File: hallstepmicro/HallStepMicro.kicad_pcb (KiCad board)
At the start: 2 copper layers, 25.4 x 55.9 mm, 30 parts, among them IC1 ATTINY84A-SS

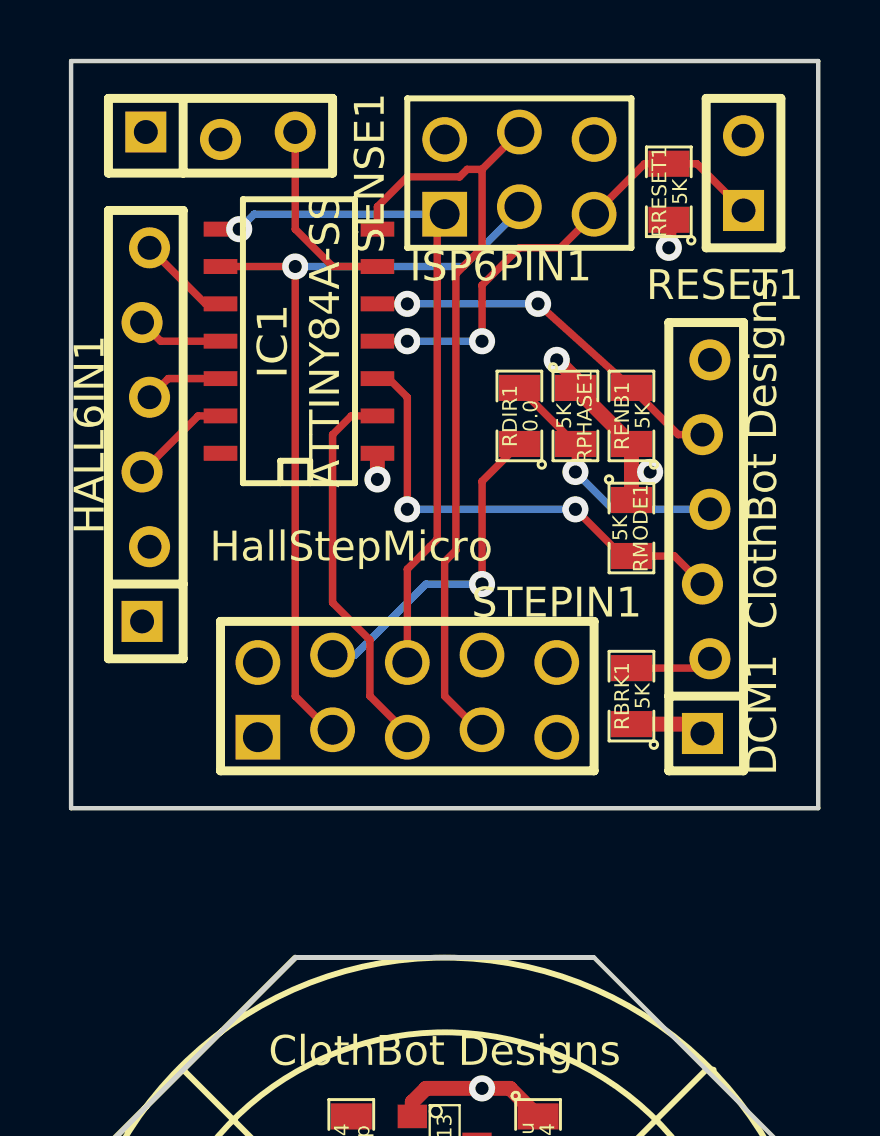
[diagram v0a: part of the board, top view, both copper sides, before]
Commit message: Moving two boards against each other.
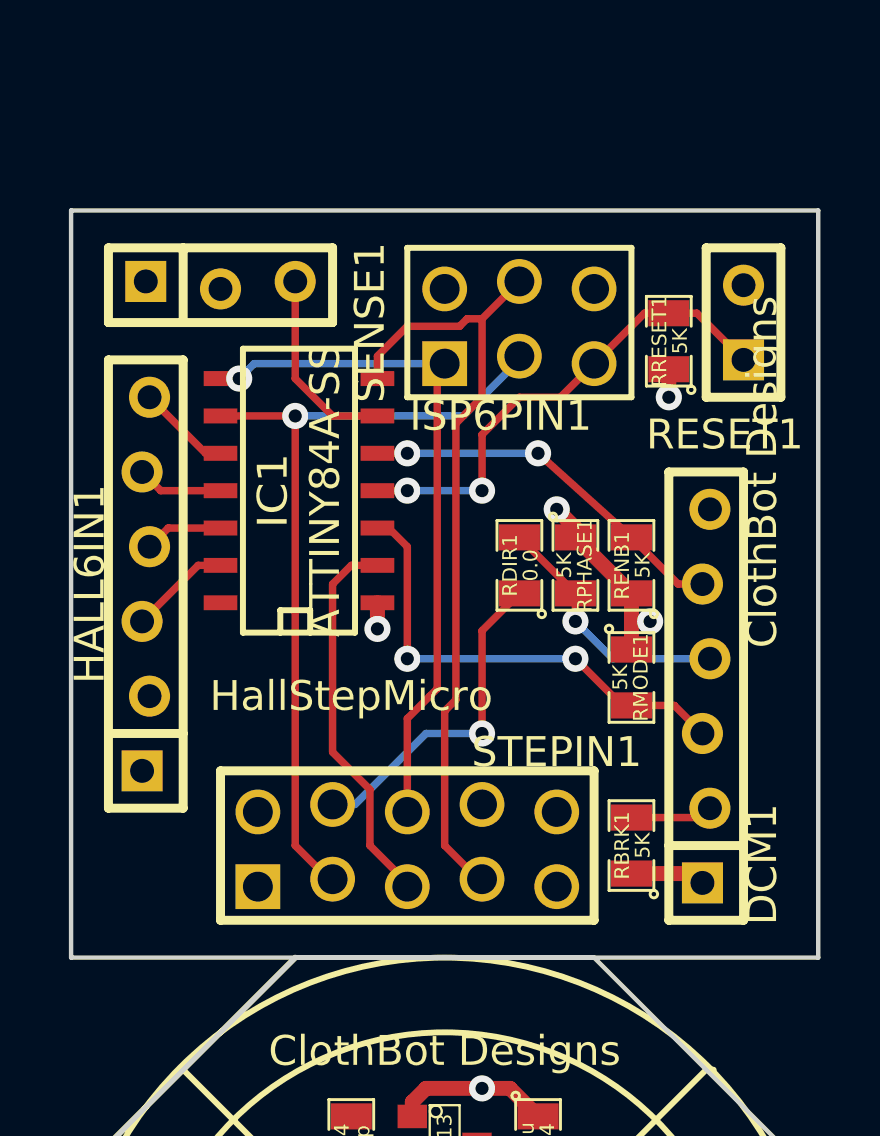
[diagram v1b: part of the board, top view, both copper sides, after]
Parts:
- moved DCM1 5.08 mm to (135.9, 54.6)
- moved HALL6IN1 5.08 mm to (116.8, 50.8)
- moved IC1 5.08 mm to (121.9, 47.6)
- moved ISP6PIN1 5.08 mm to (129.5, 41.9)
- moved RBRK1 5.08 mm to (133.3, 59.7)
- moved RDIR1 5.08 mm to (129.5, 50.2)
- moved RENB1 5.08 mm to (133.3, 50.2)
- moved RESET1 5.08 mm to (137.2, 41.9)
- moved RMODE1 5.08 mm to (133.3, 54.0)
- moved RPHASE1 5.08 mm to (131.4, 50.2)
- moved RRESET1 5.08 mm to (134.6, 42.5)
- moved SENSE1 5.08 mm to (119.4, 40.6)
- moved STEPIN1 5.08 mm to (125.7, 59.7)
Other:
- board size 25.4 x 55.9 mm -> 25.4 x 50.8 mm

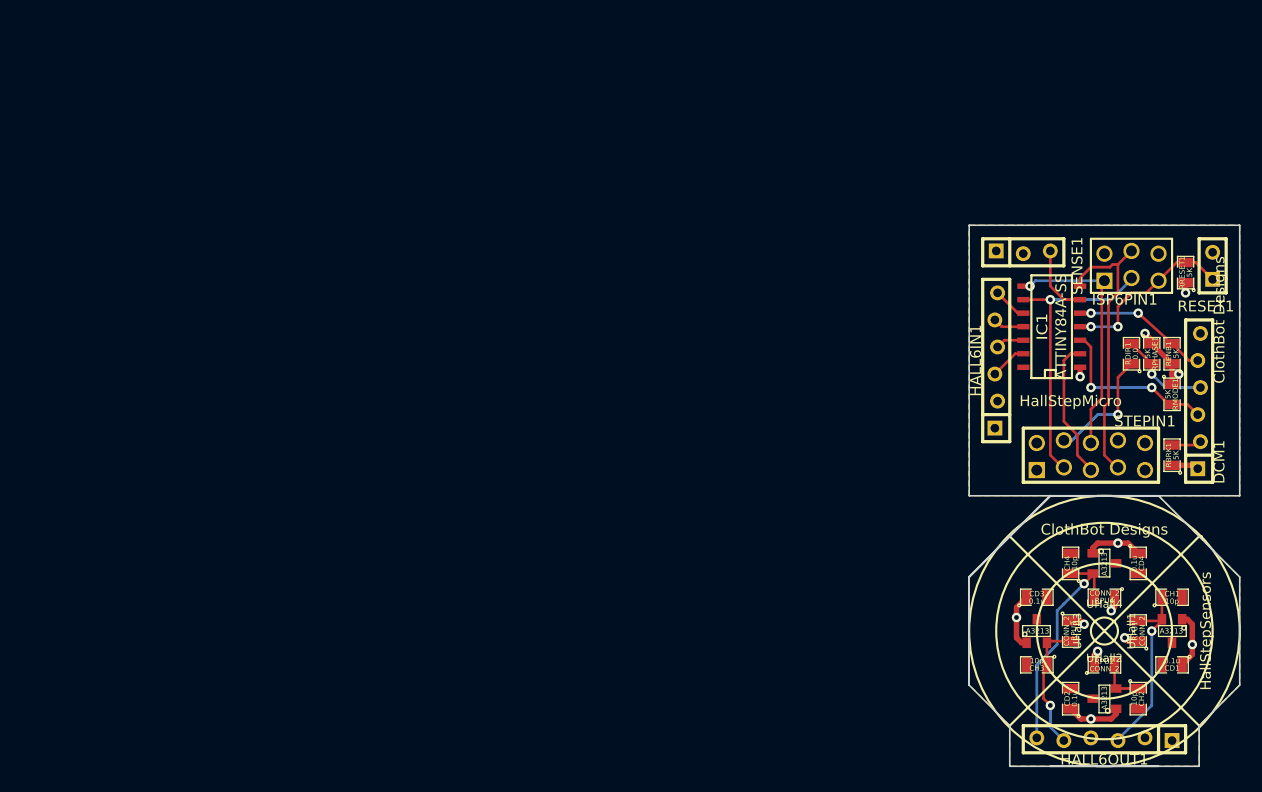
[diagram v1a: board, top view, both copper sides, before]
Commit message: Repositioned boards for right-angle cuts and cleaned up silkscreen layers.
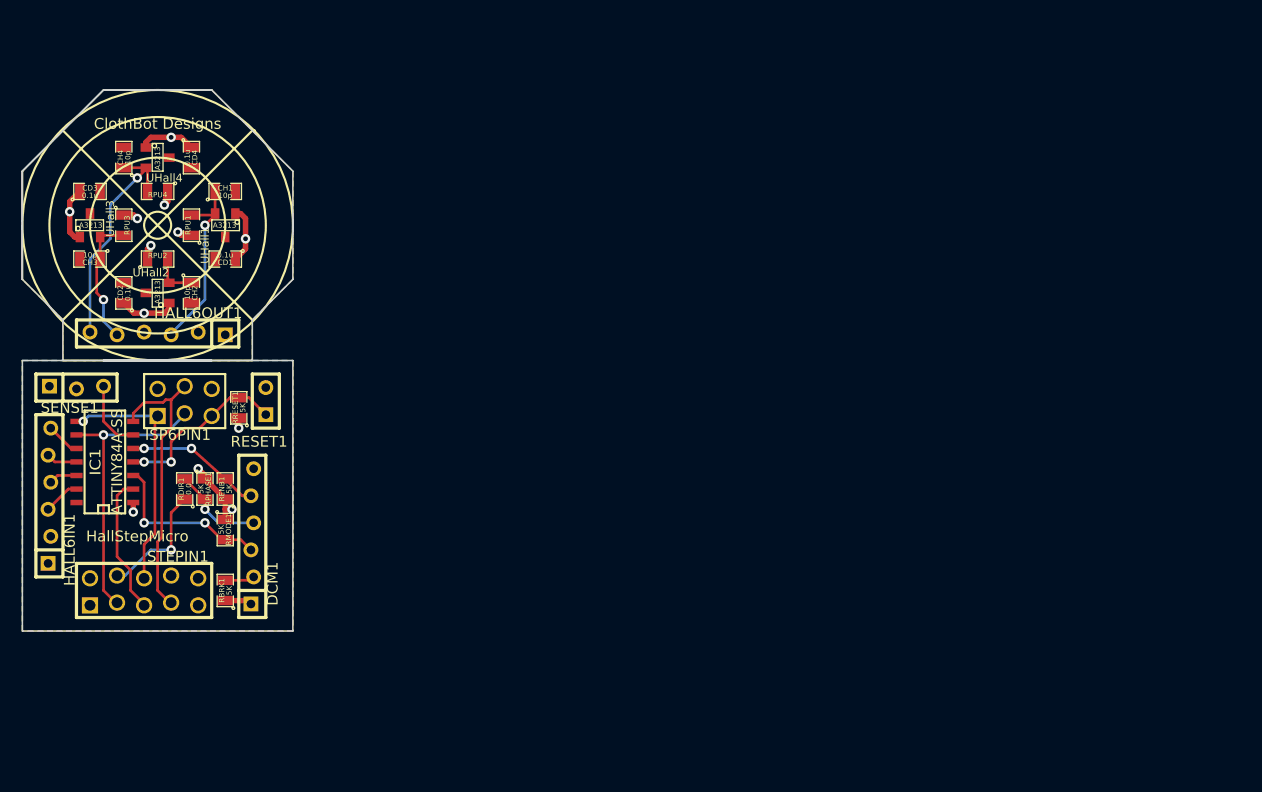
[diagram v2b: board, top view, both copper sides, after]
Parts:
- moved CD2 96.7 mm to (34.9, 44.5)
- moved CD3 96.7 mm to (31.8, 34.9)
- moved CD4 96.7 mm to (41.3, 31.8)
- moved CH2 96.7 mm to (41.3, 44.5)
- moved CH3 96.7 mm to (31.8, 41.3)
- moved CH4 96.7 mm to (34.9, 31.8)
- moved HALL6OUT1 96.7 mm to (38.1, 48.3)
- moved RPU1 96.7 mm to (41.3, 38.1)
- moved RPU2 96.7 mm to (38.1, 41.3)
- moved RPU3 96.7 mm to (34.9, 38.1)
- moved RPU4 96.7 mm to (38.1, 34.9)
- moved UHall2 96.7 mm to (38.1, 44.5)
- moved UHall3 96.7 mm to (31.8, 38.1)
- moved UHall4 96.7 mm to (38.1, 31.8)
- moved CD1 96.7 mm to (44.5, 41.3)
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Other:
- outline, holes or cut-outs redrawn

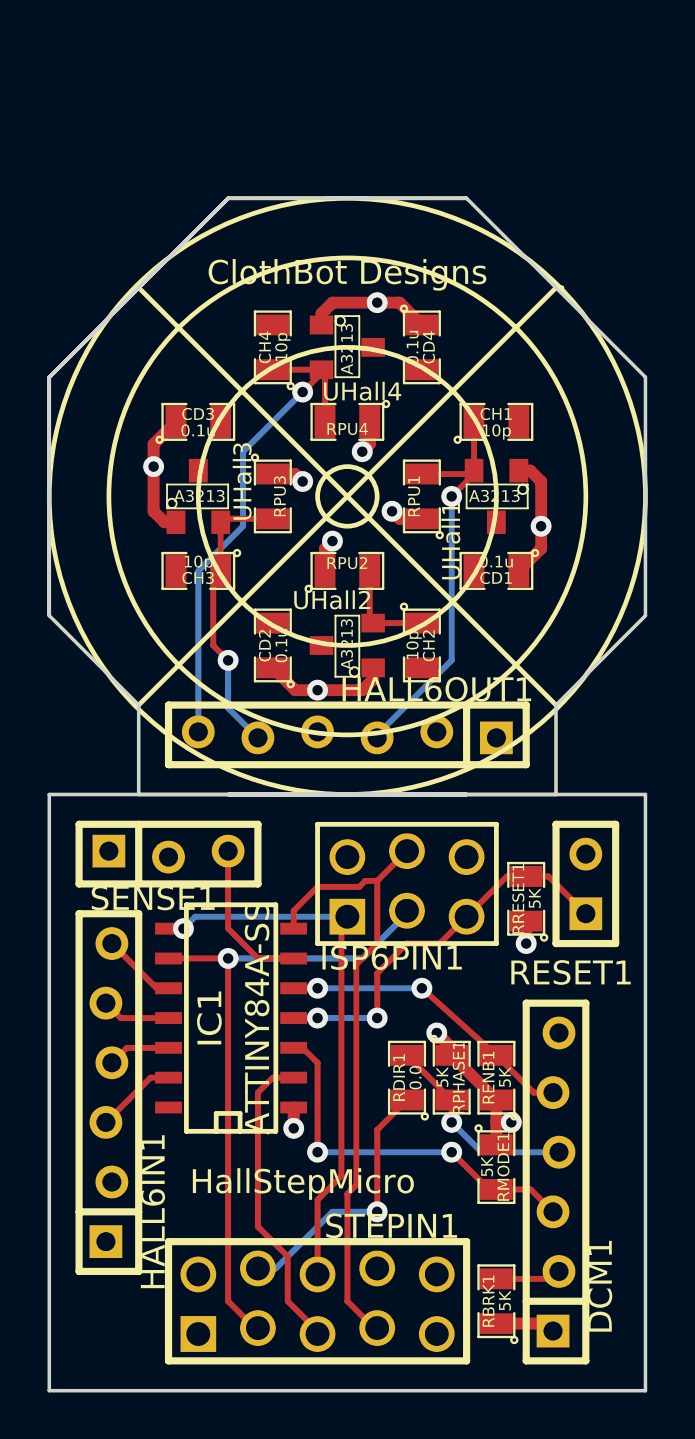
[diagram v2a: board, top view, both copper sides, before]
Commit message: Resizing edges to come under 2"x1"
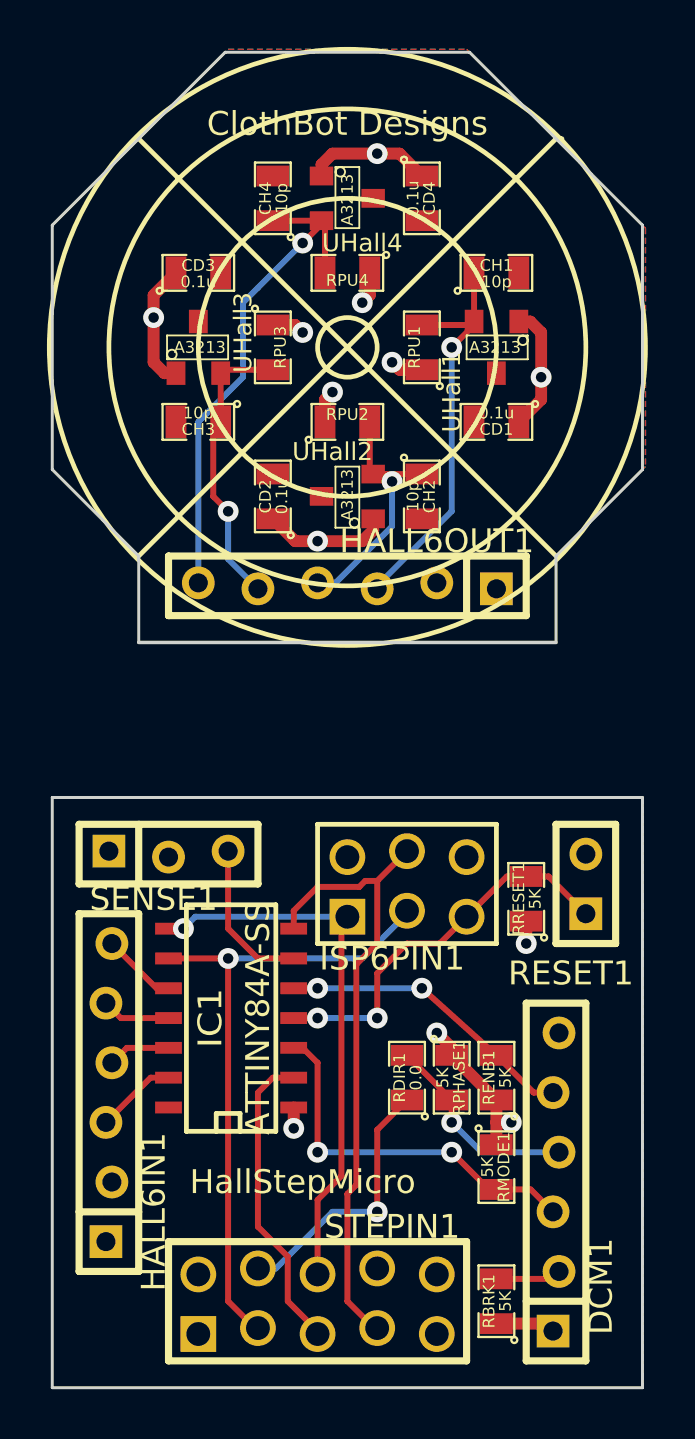
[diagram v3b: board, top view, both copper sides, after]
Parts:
- moved CD1 6.35 mm to (44.5, 34.9)
- moved CD2 6.35 mm to (34.9, 38.1)
- moved CD4 6.35 mm to (41.3, 25.4)
- moved CH2 6.35 mm to (41.3, 38.1)
- moved CH3 6.35 mm to (31.8, 34.9)
- moved CH4 6.35 mm to (34.9, 25.4)
- moved HALL6OUT1 6.35 mm to (38.1, 41.9)
- moved RPU1 6.35 mm to (41.3, 31.8)
- moved RPU2 6.35 mm to (38.1, 34.9)
- moved RPU3 6.35 mm to (34.9, 31.8)
- moved UHall1 6.35 mm to (44.5, 31.8)
- moved UHall2 6.35 mm to (38.1, 38.1)
- moved UHall3 6.35 mm to (31.8, 31.8)
- moved UHall4 6.35 mm to (38.1, 25.4)
- moved CD3 6.35 mm to (31.8, 28.6)
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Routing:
- net /HallSensors1/hall2: track 4.36 -> 11.4 mm, vias 0 -> 1
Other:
- board size 25.4 x 50.8 mm -> 25.1 x 56.9 mm

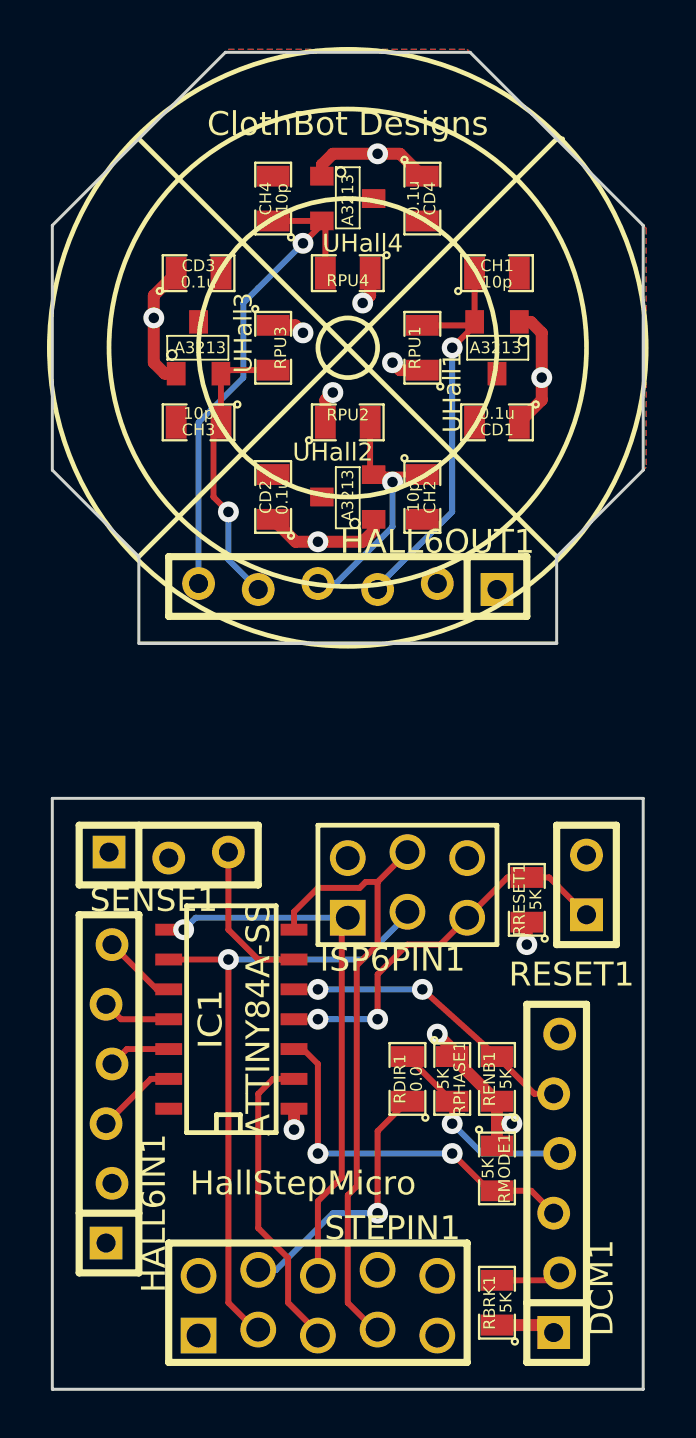
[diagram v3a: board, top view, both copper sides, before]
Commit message: Added extra clearance to copper pour
Dimension problem was probably too-large silk screen, but explicitly
satisfying DRC is a good thing anyway.
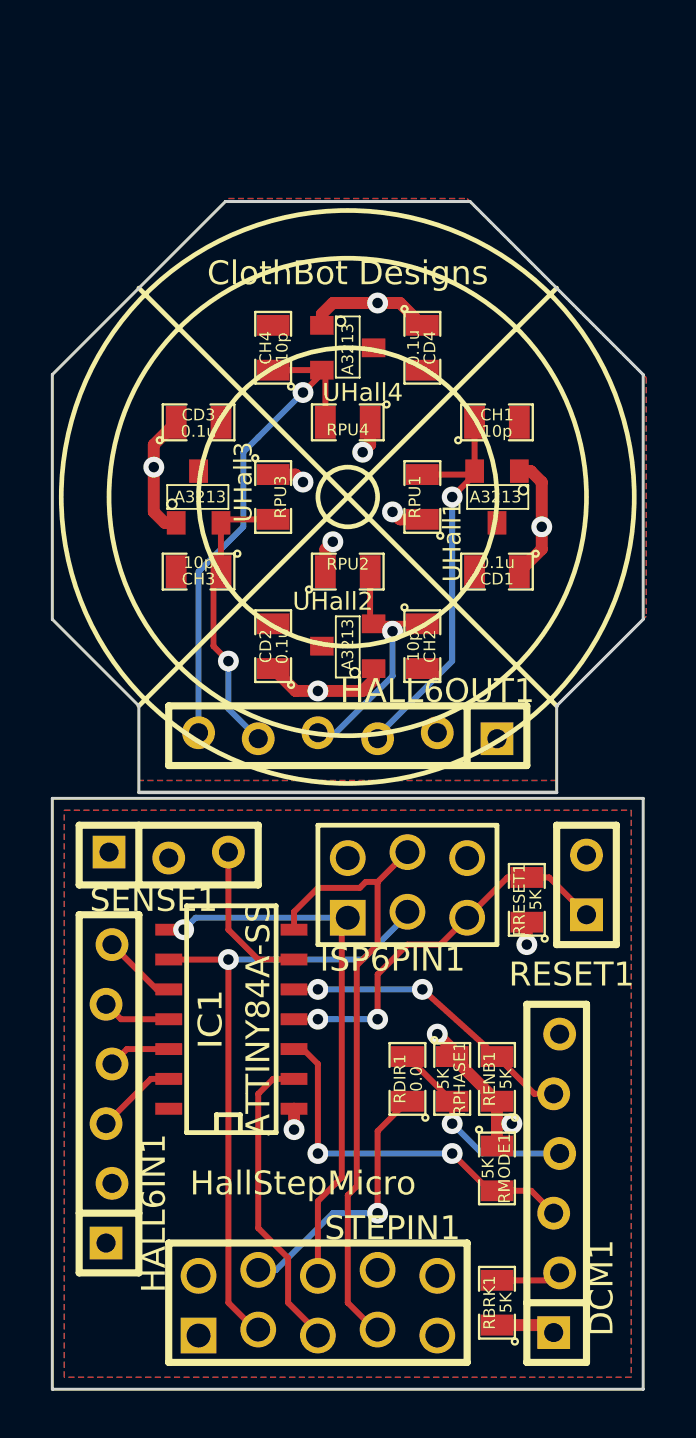
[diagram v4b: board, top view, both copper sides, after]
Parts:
- moved CD1 6.35 mm to (44.5, 41.3)
- moved CD2 6.35 mm to (34.9, 44.5)
- moved CD4 6.35 mm to (41.3, 31.8)
- moved CH2 6.35 mm to (41.3, 44.5)
- moved CH3 6.35 mm to (31.8, 41.3)
- moved CH4 6.35 mm to (34.9, 31.8)
- moved HALL6OUT1 6.35 mm to (38.1, 48.3)
- moved RPU1 6.35 mm to (41.3, 38.1)
- moved RPU2 6.35 mm to (38.1, 41.3)
- moved RPU3 6.35 mm to (34.9, 38.1)
- moved UHall1 6.35 mm to (44.5, 38.1)
- moved UHall2 6.35 mm to (38.1, 44.5)
- moved UHall3 6.35 mm to (31.8, 38.1)
- moved UHall4 6.35 mm to (38.1, 31.8)
- moved CD3 6.35 mm to (31.8, 34.9)
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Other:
- board size 25.1 x 56.9 mm -> 25.1 x 50.5 mm
